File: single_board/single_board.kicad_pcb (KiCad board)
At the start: 4 copper layers, 124.9 x 93.4 mm, 126 parts, among them J1 SWD, J11 SPI Debug, J17 BOOTSEL, J2 USB_C_Receptacle_USB2.0_16P, J3 RST, J30 JST_GH_H, J31 JST_GH_H, J32 PB_Vertical, J33 JST_GH_H, J34 PB_Vertical, J35 JST_GH_H, J36 JST_GH_H, J37 JST_GH_H, J38 PB_Vertical, J39 PB_Vertical, J40 PB_Vertical, J41 PB_Vertical, J42 PB_Vertical, J43 PB_Vertical, J44 PB_Vertical, J45 PB_Vertical, J46 PB_Vertical, J47 PB_Vertical, J48 PB_Vertical, J49 PB_Vertical, J5 JST-GH, J50 PB_Vertical, J6 Conn_01x02, Q1 AO3400A, Q3 AO3401A, Q6 AO3401A, SW1 Button, U1 AP2112K-3.3, U3 USBLC6-2SC6, U4 LSM6DSV, U5 STM32G474VBTx, Y1 FC-135

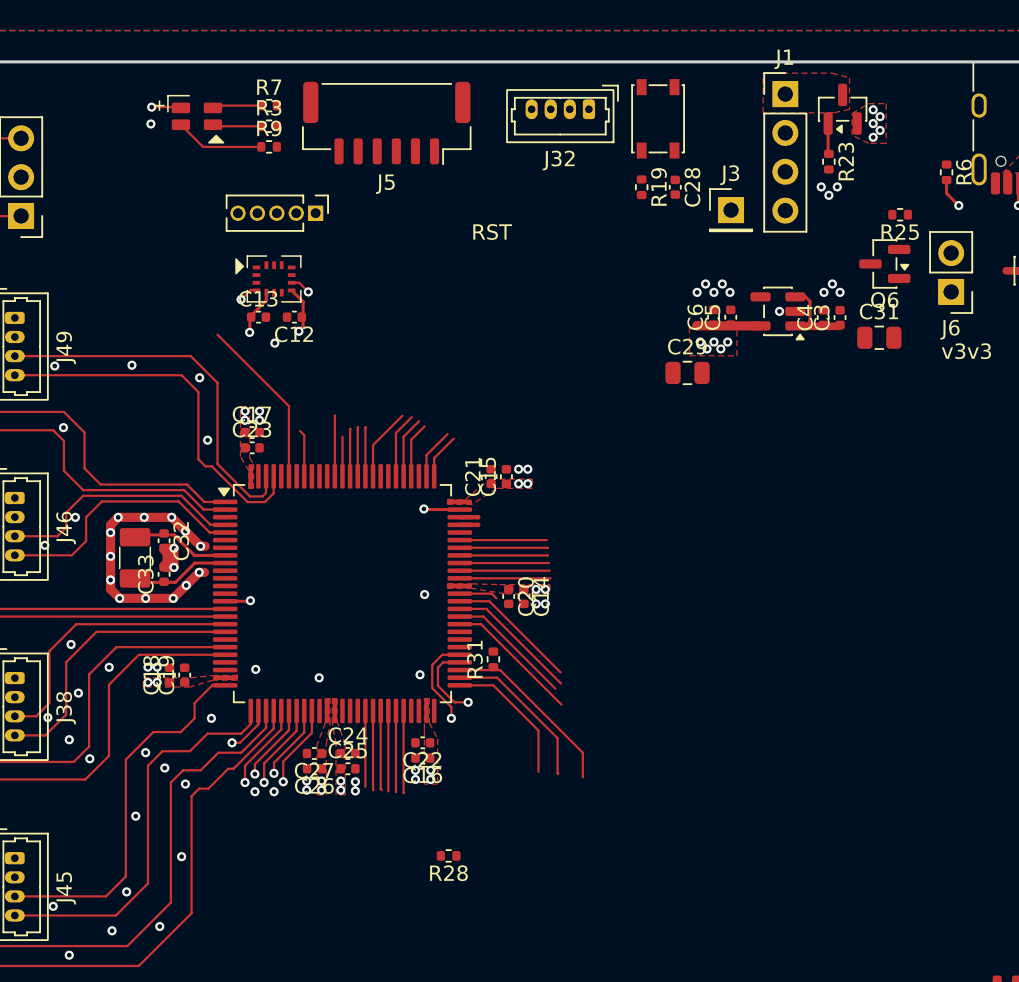
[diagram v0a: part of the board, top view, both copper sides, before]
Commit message: Update footprints in project files
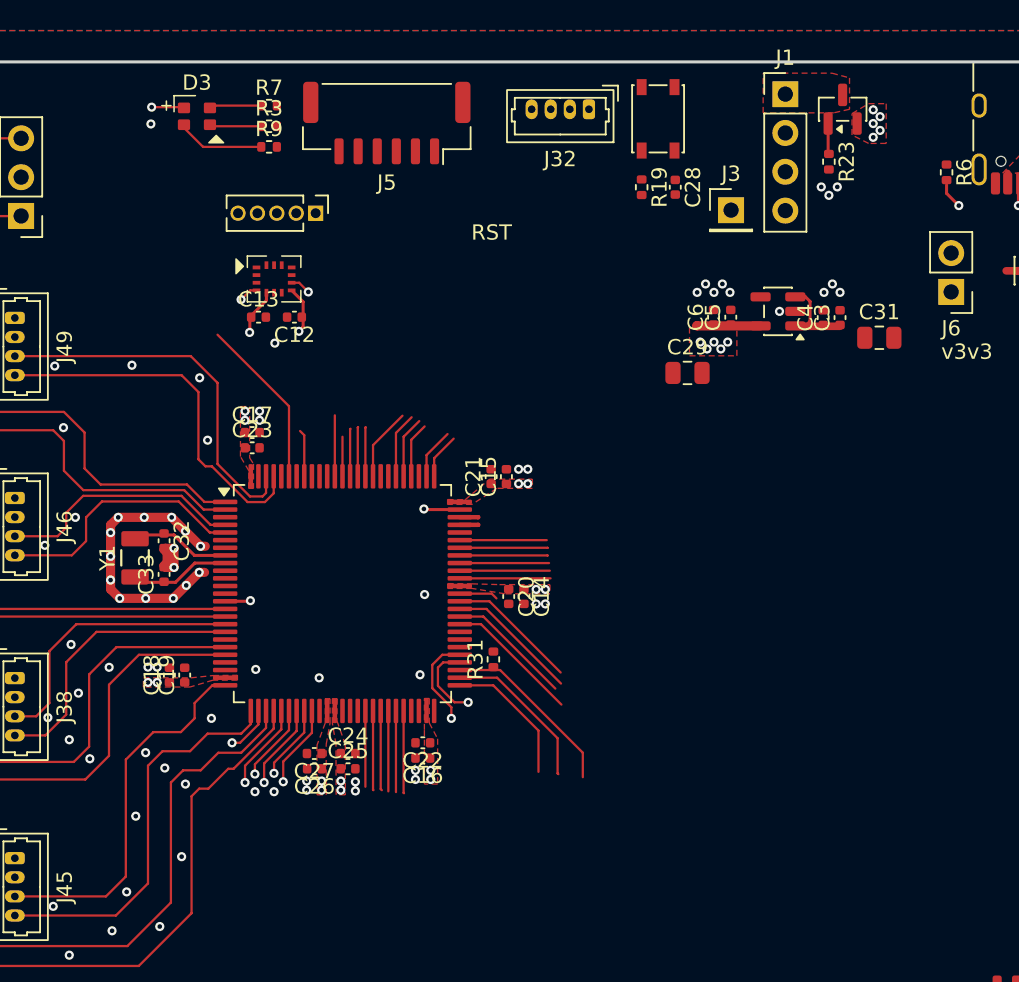
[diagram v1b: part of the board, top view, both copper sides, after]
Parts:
- removed Q6: AO3401A, Package_TO_SOT_SMD:SOT-23
- removed R25, R28: 10k, Resistor_SMD:R_0402_1005Metric
- D3: footprint Rover:FM-B2020RGBA-HG Hand Solder -> rover:FM-B2020RGBA-HG Hand Solder
- Y1: footprint Rover:FC-135 Hand Solder -> rover:FC-135

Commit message: Reset Pin to 1x02
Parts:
- removed J3: RST, Connector_PinHeader_2.54mm:PinHeader_1x01_P2.54mm_Vertical
- added J4: RST, Connector_PinHeader_2.54mm:PinHeader_1x02_P2.54mm_Vertical, F.Cu at (175.0, 82.8)
- D1: footprint Package_TO_SOT_SMD:SOT-23 -> rover:zener-3v6-onsemi-MMBZ5227BLT1G

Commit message: Schematic Changes
HSE 16 MHz
Major Pinout Change
Fix 5V LDO jumper topology
Change Mode LED
Encoder type split
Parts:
- removed C32, C33: 10pF, Capacitor_SMD:C_0402_1005Metric
- removed Y1: FC-135, rover:FC-135
- added Y2: ABM8-16MHz, Crystal:Crystal_SMD_Abracon_ABM8G-4Pin_3.2x2.5mm, F.Cu at (105.1, 105.4)
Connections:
- U5 pad 12: unconnected-(U5-PF0-Pad12) -> /OSC_IN
- U5 pad 13: unconnected-(U5-PF1-Pad13) -> /OSC_OUT
- U5 pad 8: /OSC32_IN -> unconnected-(U5-PC14-Pad8)
- U5 pad 9: /OSC32_OUT -> unconnected-(U5-PC15-Pad9)
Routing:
- net /ENC3_B: track 39.0 -> 0.00 mm
- net /ENC3_A: track 38.0 -> 0.00 mm
- net /ENC2_B: track 29.7 -> 0.00 mm
- net /ENC2_A: track 29.6 -> 0.00 mm
- net /ENC6_A: track 28.4 -> 0.00 mm
- net /ENC6_B: track 27.7 -> 0.00 mm
- net /DIR2: track 26.0 -> 0.00 mm
- net /ENC1_A: track 25.0 -> 0.00 mm
- net /ENC1_B: track 24.7 -> 0.00 mm
- net /PWM2: track 24.5 -> 0.00 mm
- net /PWM6: track 24.5 -> 0.00 mm
- net /DIR6: track 24.3 -> 0.00 mm
- net /DIR1: track 18.6 -> 0.00 mm
- net /PWM1: track 18.2 -> 0.00 mm
- net /DIR3: track 17.0 -> 0.00 mm
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
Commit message: layout positioning
spacing and positioning
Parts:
- removed D3: FM-B2020RGBA-HG, rover:FM-B2020RGBA-HG Hand Solder
- removed J1: SWD, Connector_PinHeader_2.54mm:PinHeader_1x04_P2.54mm_Vertical
- removed J4: RST, Connector_PinHeader_2.54mm:PinHeader_1x02_P2.54mm_Vertical
- added C35: 10pF, Capacitor_SMD:C_0402_1005Metric, F.Cu at (97.7, 83.1)
- added C36: 10pF, Capacitor_SMD:C_0402_1005Metric, F.Cu at (97.7, 80.9)
- added D5: TJ-S1615CY6TGLCCSRGB-A5, rover:TOGAILED, F.Cu at (152.7, 95.6)
- added J3: SWD, Connector_PinHeader_2.54mm:PinHeader_1x05_P2.54mm_Vertical, F.Cu at (135.8, 43.3)
- J32: value PB_Vertical -> ~; footprint Connector_Molex:Molex_PicoBlade_53047-0410_1x04_P1.25mm_Vertical -> Connector_PinHeader_2.54mm:PinHeader_1x04_P2.54mm_Vertical
- moved R15 160.9 mm to (83.2, 35.9)
- moved J42 160.7 mm to (65.7, 90.0), turned to -90 degrees
- moved TP2 160.3 mm to (77.4, 35.9)
- moved D4 160.3 mm to (80.5, 35.9)
- moved R14 158.0 mm to (83.2, 40.5)
- moved D2 157.4 mm to (80.5, 40.5)
- moved TP1 156.9 mm to (77.5, 40.5)
- moved R37 152.2 mm to (89.8, 44.3)
- moved J43 151.6 mm to (65.7, 112.4), turned to -90 degrees
- moved C10 150.9 mm to (87.2, 41.3), turned to -90 degrees
- moved J35 147.1 mm to (108.3, 37.8), turned to 180 degrees
- moved C30 145.4 mm to (95.0, 41.4), turned to -90 degrees
- moved D1 144.9 mm to (90.2, 41.4)
- moved J48 142.5 mm to (75.0, 101.2), turned to -90 degrees
- moved J47 142.1 mm to (75.0, 90.0), turned to -90 degrees
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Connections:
- C11 pad 1: /VBUS -> 5V
- C3 pad 1: 5V -> Net-(J6-Pin_1)
- C31 pad 1: 5V -> Net-(J6-Pin_1)
- C4 pad 1: 5V -> Net-(J6-Pin_1)
- D2 pad 1: GND -> Net-(D2-K)
- D2 pad 2: Net-(D2-A) -> 5V
- D4 pad 1: GND -> Net-(D4-K)
- D4 pad 2: Net-(D4-A) -> v3v3
- J2 pad A4: /VBUS -> 5V
- J2 pad A9: /VBUS -> 5V
- J2 pad B4: /VBUS -> 5V
- J2 pad B9: /VBUS -> 5V
- J32 pad 2: /UART4_TX -> /USART1_TX
- J32 pad 3: /UART4_RX -> /USART1_RX
- J39 pad 1: /ENC1_A -> 5V
- J39 pad 2: /ENC1_B -> /ENC1_A
- J39 pad 3: 5V -> /ENC1_B
- J40 pad 1: /ENC2_A -> 5V
- J40 pad 2: /ENC2_B -> /ENC2_A
- J40 pad 3: 5V -> /ENC2_B
- J41 pad 1: /ENC3_A -> 5V
- J41 pad 2: /ENC3_B -> /ENC3_A
- J41 pad 3: 5V -> /ENC3_B
- J42 pad 1: /ENC4_A -> 5V
- J42 pad 2: /ENC4_B -> /ENC4_A
- J42 pad 3: 5V -> /ENC4_B
- J43 pad 1: /ENC5_A -> 5V
- J43 pad 2: /ENC5_B -> /ENC_5
- J43 pad 3: 5V -> GND
- J43 pad 4: GND -> unconnected-(J43-Pin_4-Pad4)
- J44 pad 1: /ENC6_A -> 5V
- J44 pad 2: /ENC6_B -> /ENC_6
- J44 pad 3: 5V -> GND
- J44 pad 4: GND -> unconnected-(J44-Pin_4-Pad4)
- J5 pad 3: /UART5_TX -> /USART3_TX
- J5 pad 4: /UART5_RX -> /USART3_RX
- J6 pad 1: 5V -> Net-(J6-Pin_1)
- J6 pad 2: /VBUS -> 5V
- R14 pad 1: 5V -> Net-(D2-K)
- R14 pad 2: Net-(D2-A) -> GND
- R15 pad 1: v3v3 -> Net-(D4-K)
- R15 pad 2: Net-(D4-A) -> GND
- R3 pad 1: Net-(D3-RK) -> /TRI_LED_B
- R3 pad 2: /TRI_LED_R -> Net-(D5-BA)
- R7 pad 1: Net-(D3-GK) -> /TRI_LED_G
- R7 pad 2: /TRI_LED_G -> Net-(D5-GA)
- R9 pad 1: Net-(D3-BK) -> /TRI_LED_R
- R9 pad 2: /TRI_LED_B -> Net-(D5-RA)
- U1 pad 1: 5V -> Net-(J6-Pin_1)
- U1 pad 3: 5V -> Net-(J6-Pin_1)
- U3 pad 5: /VBUS -> 5V
- U5 pad 1: /ENC6_A -> /ENC3_A
- U5 pad 15: /ENC1_A -> /ENC4_A
- U5 pad 16: /ENC1_B -> /ENC4_B
- U5 pad 17: /PWM1 -> /PWM4
- U5 pad 18: /DIR1 -> /DIR4
- U5 pad 19: unconnected-(U5-PF2-Pad19) -> /DIR5
- U5 pad 2: /ENC6_B -> /ENC3_B
- U5 pad 20: /ENC2_A -> /ENC_6
- U5 pad 21: /ENC2_B -> /ENC_5
- U5 pad 22: unconnected-(U5-PA2-Pad22) -> /PWM5
- U5 pad 25: /PWM2 -> /PWM6
- U5 pad 26: /DIR2 -> /DIR6
- U5 pad 27: /LED1 -> /IMU_SCK
- U5 pad 28: /ENC3_A -> /IMU_MISO
- U5 pad 29: /ENC3_B -> /IMU_MOSI
- U5 pad 3: unconnected-(U5-PE4-Pad3) -> /PWM3
- U5 pad 30: /LED2 -> /IMU_NSS
- U5 pad 31: /LED3 -> /INT1
- U5 pad 32: /LED4 -> /INT2
- U5 pad 33: /LED5 -> unconnected-(U5-PB1-Pad33)
- U5 pad 34: /LED6 -> unconnected-(U5-PB2-Pad34)
- U5 pad 4: /PWM3 -> /DIR3
- U5 pad 42: unconnected-(U5-PE11-Pad42) -> /LASER_SIG
- U5 pad 46: /LASER_SIG -> unconnected-(U5-PE15-Pad46)
- U5 pad 5: /DIR3 -> unconnected-(U5-PE6-Pad5)
- U5 pad 51: /CAN_RX -> /LED6
- U5 pad 52: /CAN_TX -> /LED5
- U5 pad 53: /CAN_STB -> /LED4
- U5 pad 54: /CAN_LED -> /LED3
- U5 pad 55: /HEARTBEAT -> /LED2
- U5 pad 56: unconnected-(U5-PD9-Pad56) -> /LED1
- U5 pad 57: unconnected-(U5-PD10-Pad57) -> /HEARTBEAT
- U5 pad 58: unconnected-(U5-PD11-Pad58) -> /CAN_LED
- U5 pad 59: /ENC4_A -> unconnected-(U5-PD12-Pad59)
- U5 pad 60: /ENC4_B -> unconnected-(U5-PD13-Pad60)
- U5 pad 61: /DIR5 -> unconnected-(U5-PD14-Pad61)
- U5 pad 62: /PWM5 -> unconnected-(U5-PD15-Pad62)
- U5 pad 65: /ENC5_A -> /TRI_LED_G
- U5 pad 66: /ENC5_B -> /TRI_LED_R
- U5 pad 67: /PWM4 -> /TRI_LED_B
- U5 pad 68: /DIR4 -> /I2C_SDA
- U5 pad 69: /I2C_SDA -> /I2C_SCL
- U5 pad 70: /I2C_SCL -> /USART1_TX
- U5 pad 71: unconnected-(U5-PA10-Pad71) -> /USART1_RX
- U5 pad 79: /UART4_TX -> /USART3_TX
- U5 pad 80: /UART4_RX -> /USART3_RX
- U5 pad 81: /UART5_TX -> unconnected-(U5-PC12-Pad81)
- U5 pad 82: unconnected-(U5-PD0-Pad82) -> /CAN_RX
- U5 pad 83: unconnected-(U5-PD1-Pad83) -> /CAN_TX
- U5 pad 84: /UART5_RX -> /CAN_STB
- U5 pad 85: /TRI_LED_G -> unconnected-(U5-PD3-Pad85)
- U5 pad 86: /TRI_LED_R -> unconnected-(U5-PD4-Pad86)
- U5 pad 87: /TRI_LED_B -> unconnected-(U5-PD5-Pad87)
- U5 pad 88: /INT2 -> unconnected-(U5-PD6-Pad88)
- U5 pad 89: /IMU_NSS -> unconnected-(U5-PD7-Pad89)
- U5 pad 90: /IMU_SCK -> /DIR1
- U5 pad 91: /IMU_MISO -> /ENC1_A
- U5 pad 92: /IMU_MOSI -> /ENC1_B
- U5 pad 93: /INT1 -> /ENC2_A
- U5 pad 94: unconnected-(U5-PB7-Pad94) -> /ENC2_B
- U5 pad 96: unconnected-(U5-PB9-Pad96) -> /DIR2
- U5 pad 97: /DIR6 -> /PWM1
- U5 pad 98: /PWM6 -> /PWM2
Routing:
- net /ENC1_A: track 0.00 -> 56.2 mm
- net /ENC1_B: track 0.00 -> 54.5 mm
- net /ENC2_A: track 0.00 -> 53.4 mm
- net /ENC2_B: track 0.00 -> 52.0 mm
- net /ENC_6: track 0.00 -> 50.8 mm
- net /ENC_5: track 0.00 -> 50.5 mm
- net /DIR1: track 0.00 -> 46.9 mm
- net /ENC3_A: track 0.00 -> 39.5 mm
- net /DIR6: track 0.00 -> 39.0 mm
- net /ENC3_B: track 0.00 -> 38.5 mm
- net /PWM6: track 0.00 -> 38.5 mm
- net /ENC4_B: track 0.00 -> 38.4 mm
- net /ENC4_A: track 1.40 -> 38.1 mm
- net /DIR5: track 0.00 -> 35.4 mm
- net /PWM2: track 0.00 -> 34.1 mm
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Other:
- board size 124.9 x 93.4 mm -> 102.8 x 99.7 mm

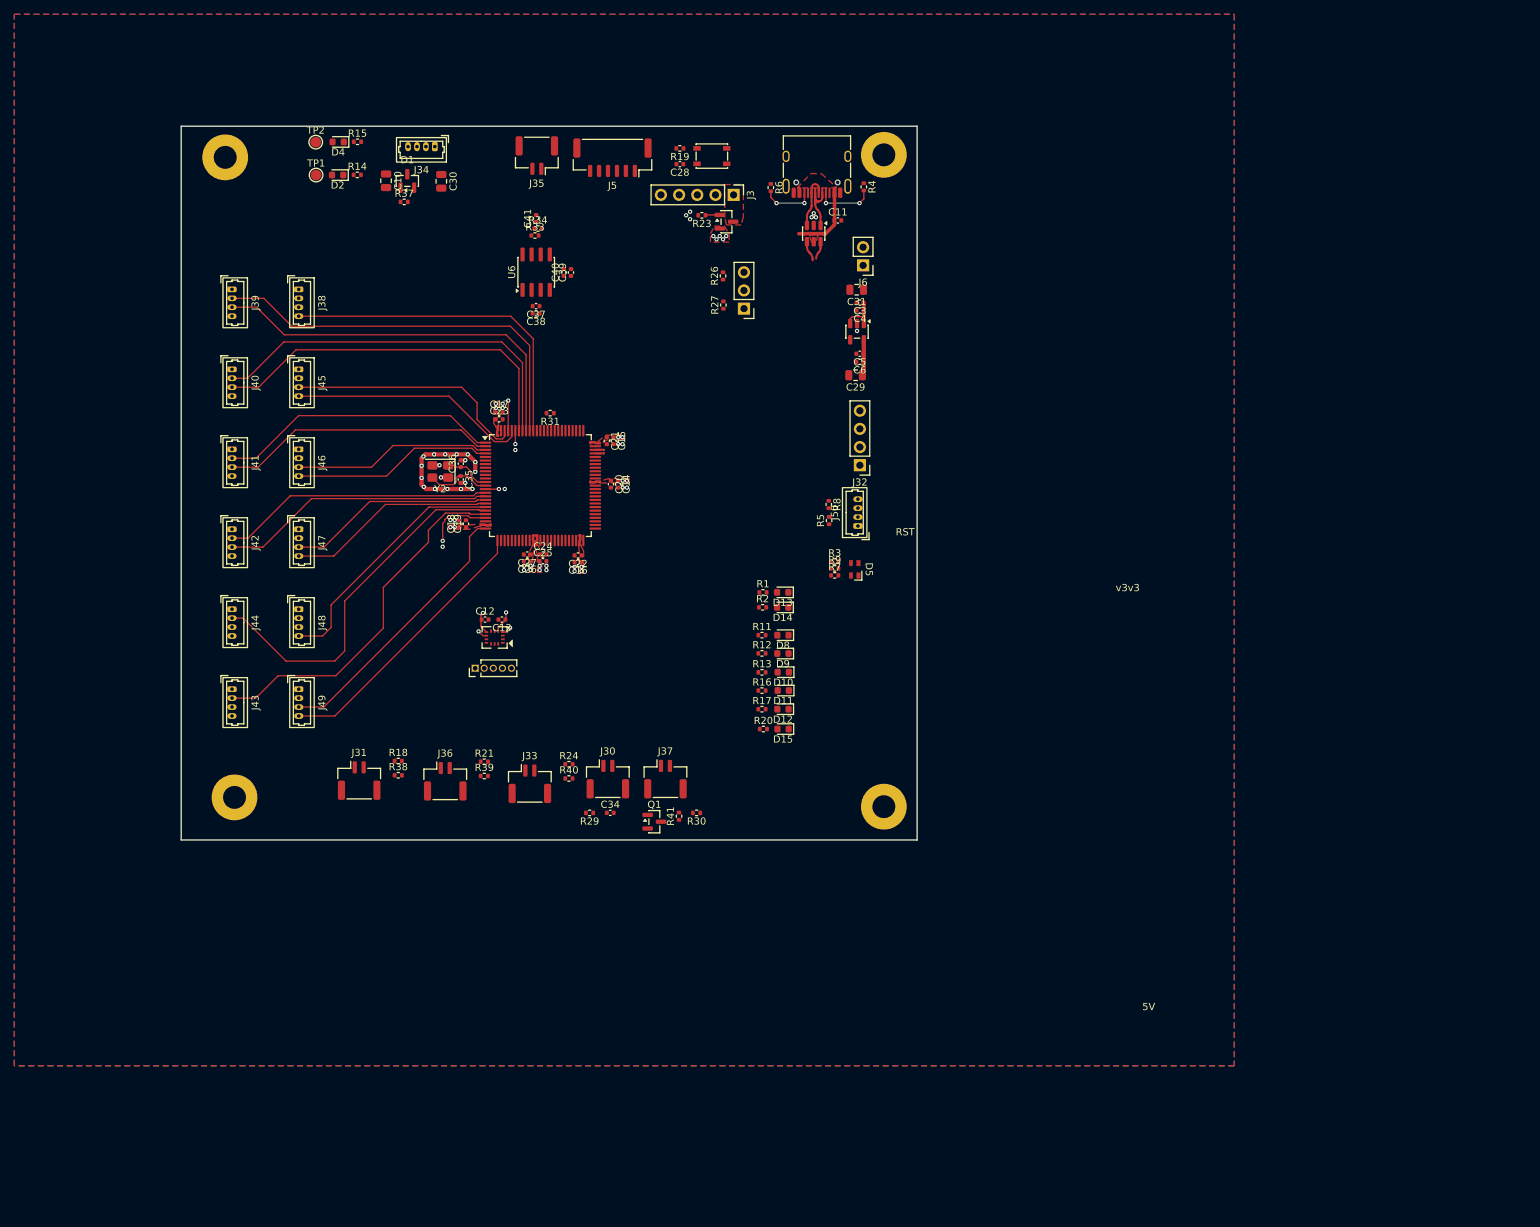
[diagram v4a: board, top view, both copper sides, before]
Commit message: LDO Power Jumper
Improved topology and usability
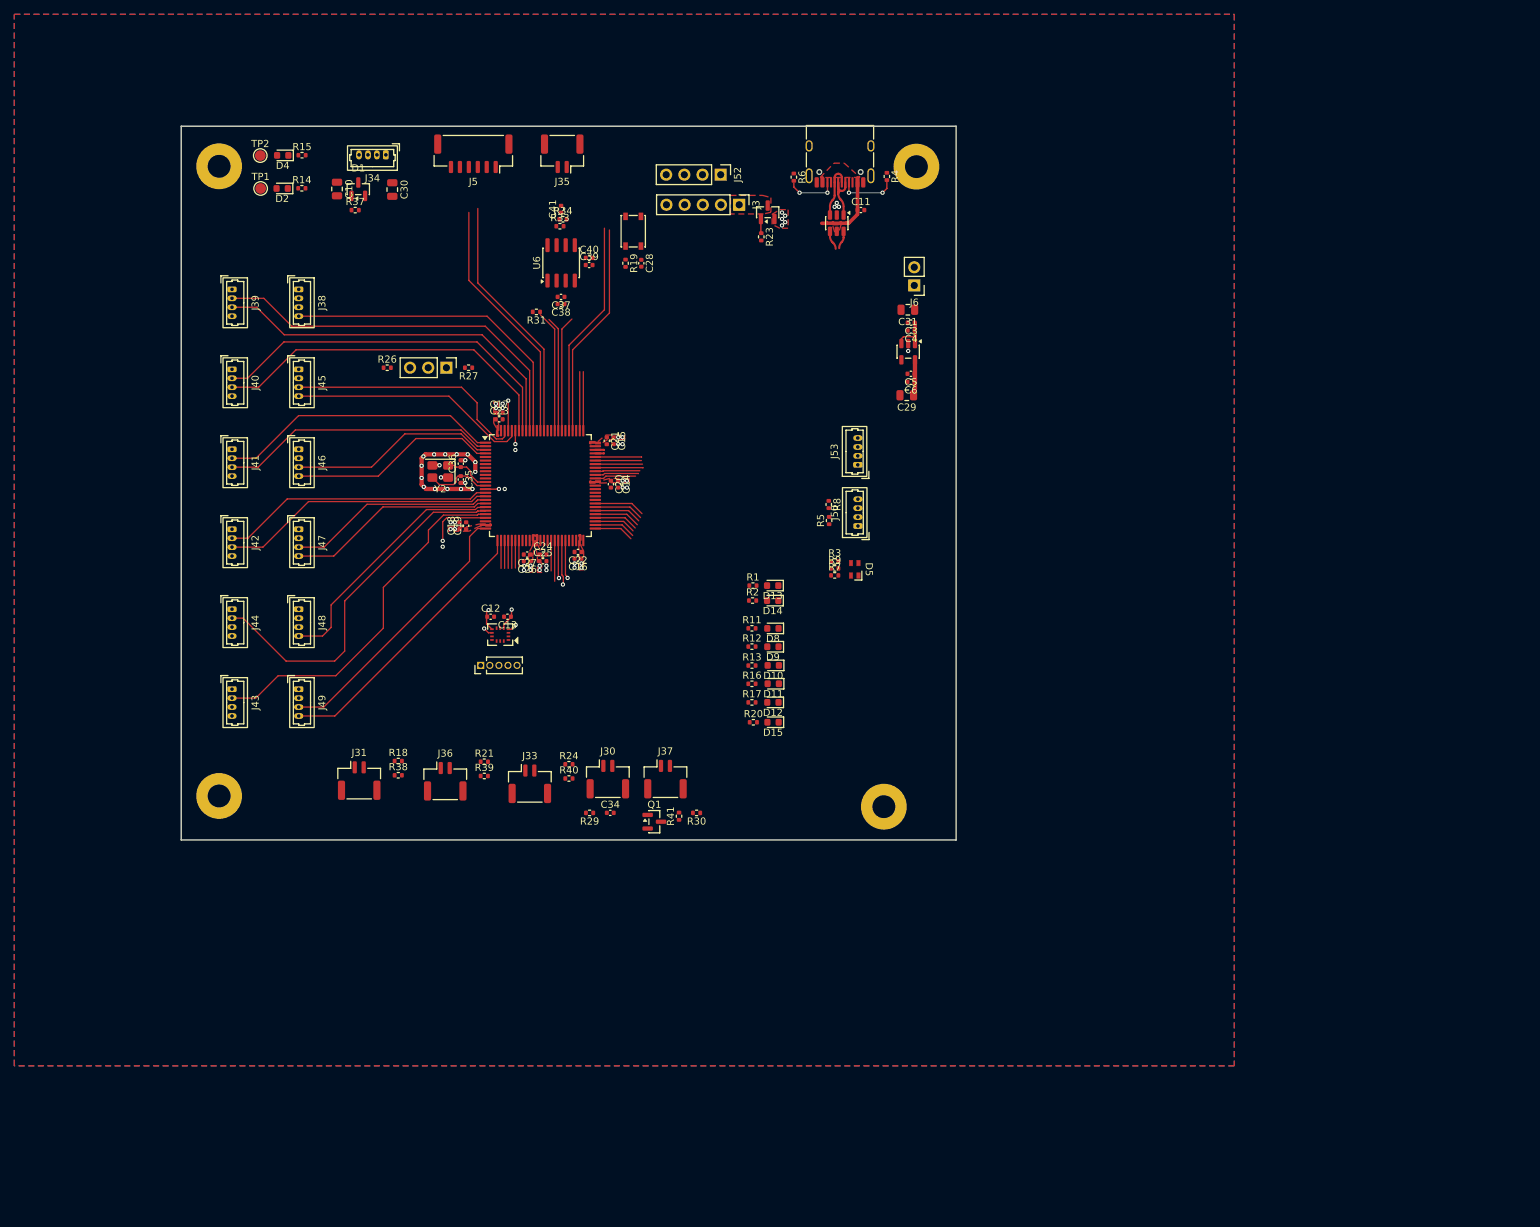
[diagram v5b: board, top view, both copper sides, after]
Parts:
- removed J32: ~, Connector_PinHeader_2.54mm:PinHeader_1x04_P2.54mm_Vertical
- added J52: ~, Connector_PinHeader_2.54mm:PinHeader_1x04_P2.54mm_Vertical, F.Cu at (134.0, 40.5)
- added J53: PB_Vertical, Connector_Molex:Molex_PicoBlade_53047-0410_1x04_P1.25mm_Vertical, F.Cu at (153.2, 81.0)
- moved R26 48.7 mm to (87.4, 67.5), turned to 0 degrees
- moved J17 42.4 mm to (95.7, 67.5), turned to -90 degrees
- moved R27 36.7 mm to (98.8, 67.5), turned to 180 degrees
- moved J5 19.5 mm to (99.4, 37.5)
- moved R19 17.8 mm to (120.7, 52.9), turned to -90 degrees
- moved SW1 15.2 mm to (121.8, 48.4), turned to 90 degrees
- moved C28 14.9 mm to (122.9, 52.9), turned to -90 degrees
- moved R31 14.3 mm to (108.2, 59.6)
- moved R23 8.82 mm to (139.7, 49.2), turned to -90 degrees
- moved D2 7.97 mm to (72.7, 42.4)
- moved D4 7.97 mm to (72.8, 37.8)
- moved R14 7.97 mm to (75.5, 42.4)
- moved R15 7.97 mm to (75.5, 37.8)
- moved TP1 7.97 mm to (69.7, 42.4)
- moved TP2 7.97 mm to (69.7, 37.8)
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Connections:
- J5 pad 3: /USART3_TX -> /USART2_TX
- J5 pad 4: /USART3_RX -> /USART2_RX
- U5 pad 87: unconnected-(U5-PD5-Pad87) -> /USART2_TX
- U5 pad 88: unconnected-(U5-PD6-Pad88) -> /USART2_RX
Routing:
- net /USART2_TX: track 0.00 -> 34.9 mm
- net /USART2_RX: track 0.00 -> 34.6 mm
- net /USART3_RX: track 0.00 -> 30.4 mm
- net /USART3_TX: track 0.00 -> 30.2 mm
- net /CAN_STB: track 0.00 -> 17.0 mm
- net /CAN_RX: track 0.00 -> 16.2 mm
- net /CAN_TX: track 0.00 -> 16.1 mm
- net /SWDIO: track 0.00 -> 8.25 mm
- net /SWCLK: track 0.00 -> 8.25 mm
- net /CAN_LED: track 0.00 -> 7.12 mm
- net /HEARTBEAT: track 0.00 -> 6.94 mm
- net /I2C_SDA: track 0.00 -> 6.69 mm
- net /LED1: track 0.00 -> 6.67 mm
- net /I2C_SCL: track 0.00 -> 6.60 mm
- net /LED2: track 0.00 -> 6.49 mm
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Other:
- board size 102.8 x 99.7 mm -> 108.3 x 99.7 mm
- board text removed: "5V"
- board text removed: "RST"
- board text removed: "v3v3"
